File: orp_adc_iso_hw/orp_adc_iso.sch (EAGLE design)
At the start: 25 parts, among them IC1 AD8603AUJZ-REEL7, IC2 LM385MX-2.5_NOPB, IC3 ADS1115IDGSR, IC4 ADUM1250ARZ, J1 RF1-01B-D-00-75

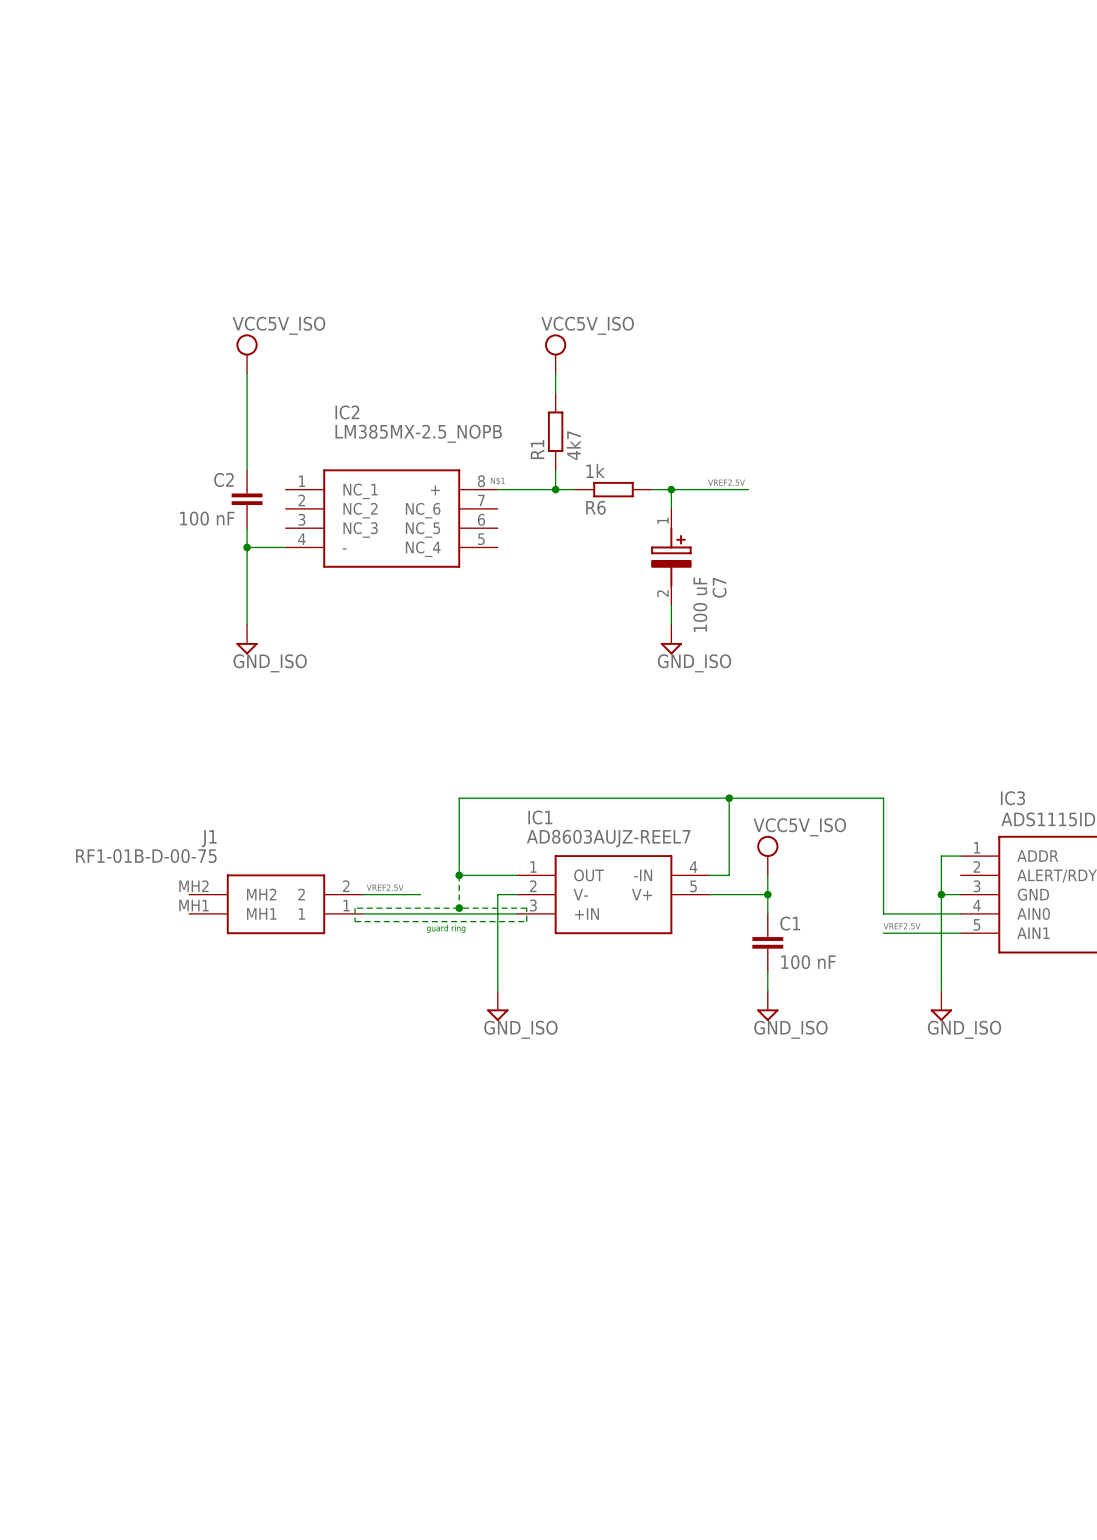
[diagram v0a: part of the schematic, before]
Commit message: used op amp in bigger IC package
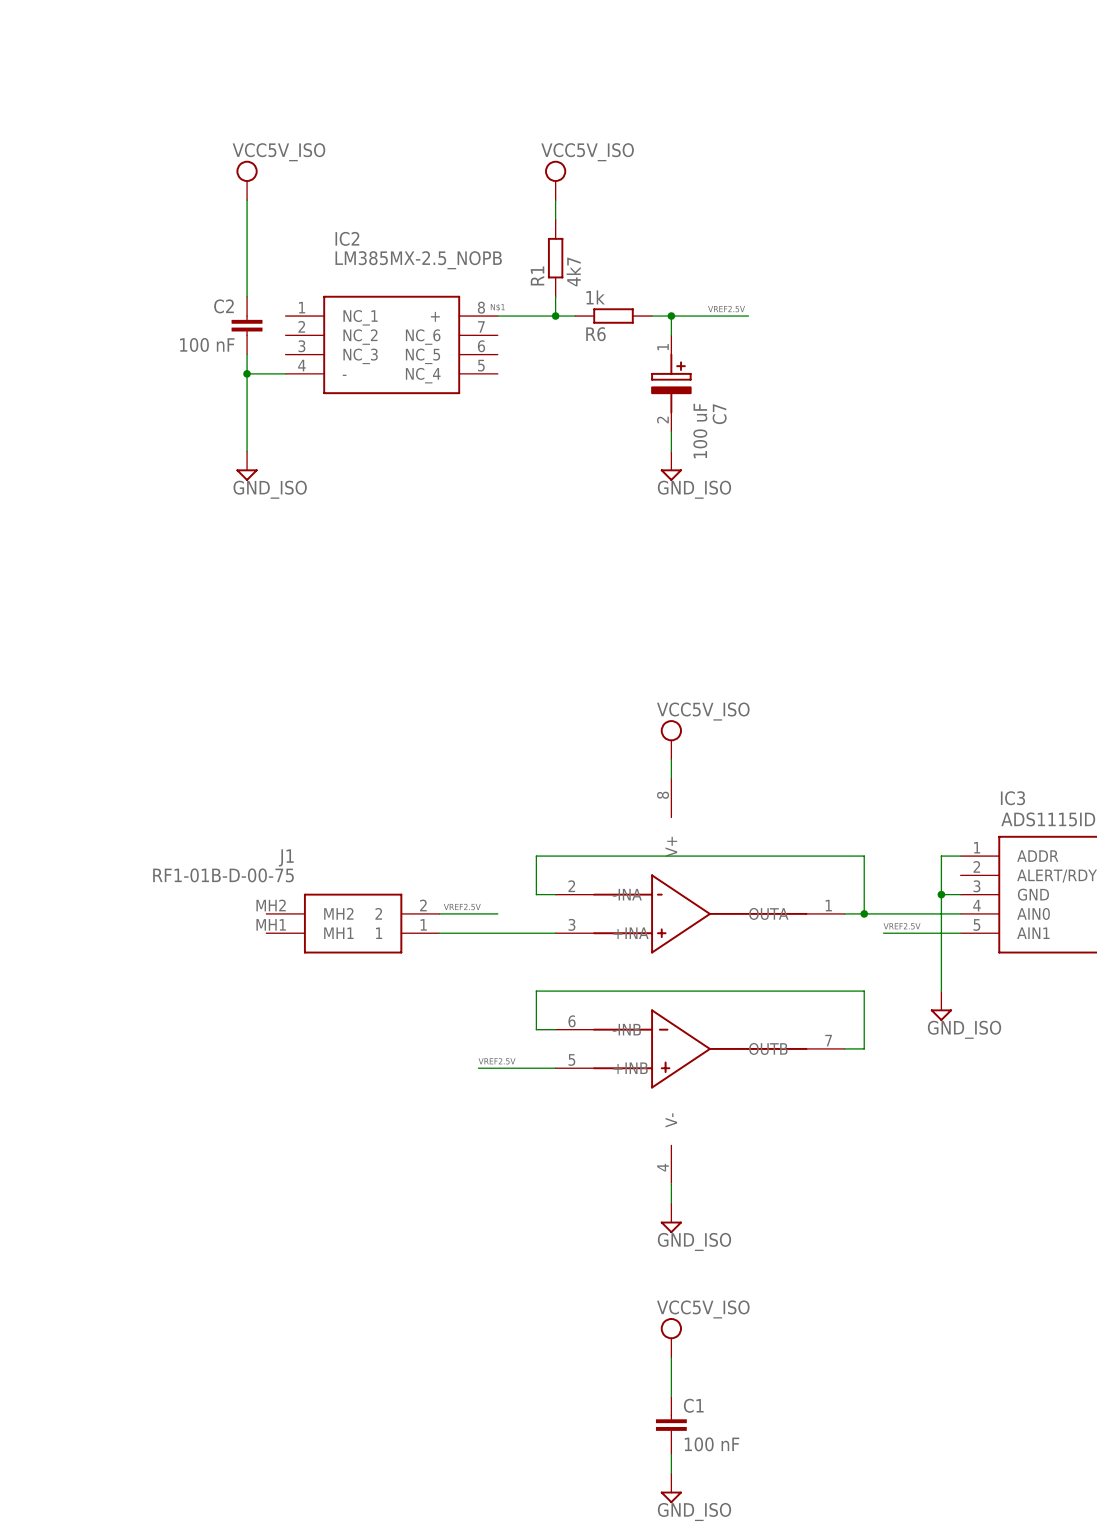
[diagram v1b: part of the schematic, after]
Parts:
- removed IC1: AD8603AUJZ-REEL7, AD8603AUJZ-REEL7:AD8603AUJZ-REEL7
- added U$1: LMC6482AIMX/NOPB, other:LMC6482AIMX/NOPB
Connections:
- new net N$4: U$1.-INB, U$1.OUTB
- net GND_ISO: now also U$1.V-; no longer IC1.V-
- net N$2: now also U$1.+INA; no longer IC1.+IN
- net N$3: now also U$1.-INA, U$1.OUTA; no longer IC1.-IN, IC1.OUT
- net VCC5V_ISO: now also U$1.V+; no longer IC1.V+
- net VREF2.5V: now also U$1.+INB
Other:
- note removed: "guard ring"
- moved on the sheet: C1, C2, C7, IC2, J1, R1, R6

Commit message: correct capacitor size used
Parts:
- removed C10: 100 uF, 293D106X9016B2TE3:293D106X9016B2TE3
- added C11, C12, C13: 100 uF, rcl:CPOL-EUSMCC
- C7, C9: value 100 uF -> 100 nF; device 293D106X9016B2TE3:293D106X9016B2TE3 -> rcl:C-EUC0603; DESCRIPTION Solid Tantalum Surface Mount Chip Capacitors TANTAMOUNT(TM)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 -> (none); HEIGHT 2.1mm -> (none); MANUFACTURER_NAME Vishay -> (none); MANUFACTURER_PART_NUMBER 293D106X9016B2TE3 -> (none)
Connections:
- net GND: now also C13.-; no longer C10.-
- net GND_ISO: now also C11.-, C12.-, C7.2, C9.2; no longer C7.-, C9.-
- net VCC5V: now also C13.+; no longer C10.+
- net VCC5V_ISO: now also C12.+; no longer C9.+
- net VREF2.5V: now also C11.+, C7.1, C9.1; no longer C7.+
